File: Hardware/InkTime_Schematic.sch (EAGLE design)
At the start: 105 parts, among them IC1 BQ25180YBGR_BQ25180YBGR, IC2 RT6160AWSC_RT6160AWSC, IC3 BMA423_BMA423, IC4 DRV2605YZFR_DRV2605YZFR, J1 TC2030-IDC_TC2030-IDC, J2 503480-2400_503480-2400, J3 KH-TYPE-C-16P_KH-TYPE-C-16P, P1.01/2.4B NORDIC_NRF_4_NRF52840_QF, Q2 ESP32_C6_LIBRARY_6_SI1308EDL-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, SW1 2025-10-22_07-23-44_LIBRARY_E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, SW2 2025-10-22_07-23-44_LIBRARY_E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, SW3 2025-10-22_07-23-44_LIBRARY_E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, U1 ESP32_C6_LIBRARY_MAX17048G+T10, X1 32MHz, X2 32.768KHz

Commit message: Added GND value to GND objects
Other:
- moved on the sheet: ANT1, C1-EP-DR, C10, C11, C12, C13, C15, C16, C17, C18, C2, C2-EP-DR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

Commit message: redenumire TP
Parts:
- removed TP_SDA1, TP_SDA10, TP_SDA2, TP_SDA3, TP_SDA4, TP_SDA5, TP_SDA6, TP_SDA7, TP_SDA8, TP_SDA9: HECTOR_WATCH_1_TPTP20R, InkTime_v5:HECTOR_WATCH_1_TPTP20R
- added TP_3.3V, TP_BAT_GND, TP_GND, TP_ON, TP_OP, TP_RESET, TP_SWDCLK, TP_SWDIO, TP_SWO, TP_VBAT: HECTOR_WATCH_1_TPTP20R, InkTime_v5:HECTOR_WATCH_1_TPTP20R
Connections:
- net 3V3/2.4A: now also TP_3.3V.TP; no longer TP_SDA5.TP
- net GND: now also TP_BAT_GND.TP, TP_GND.TP; no longer TP_SDA10.TP, TP_SDA6.TP
- net OUT+: now also TP_OP.TP; no longer TP_SDA7.TP
- net OUT-: now also TP_ON.TP; no longer TP_SDA8.TP
- net RESET: now also TP_RESET.TP; no longer TP_SDA4.TP
- net SWDCLK: now also TP_SWDCLK.TP; no longer TP_SDA3.TP
- net SWDIO: now also TP_SWDIO.TP; no longer TP_SDA2.TP
- net SWO: now also TP_SWO.TP; no longer TP_SDA1.TP
- net VBAT/1.2A: now also TP_VBAT.TP; no longer TP_SDA9.TP
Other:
- moved on the sheet: ANT1, C1-EP-DR, C10, C11, C12, C13, C15, C16, C17, C18, C2, C2-EP-DR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

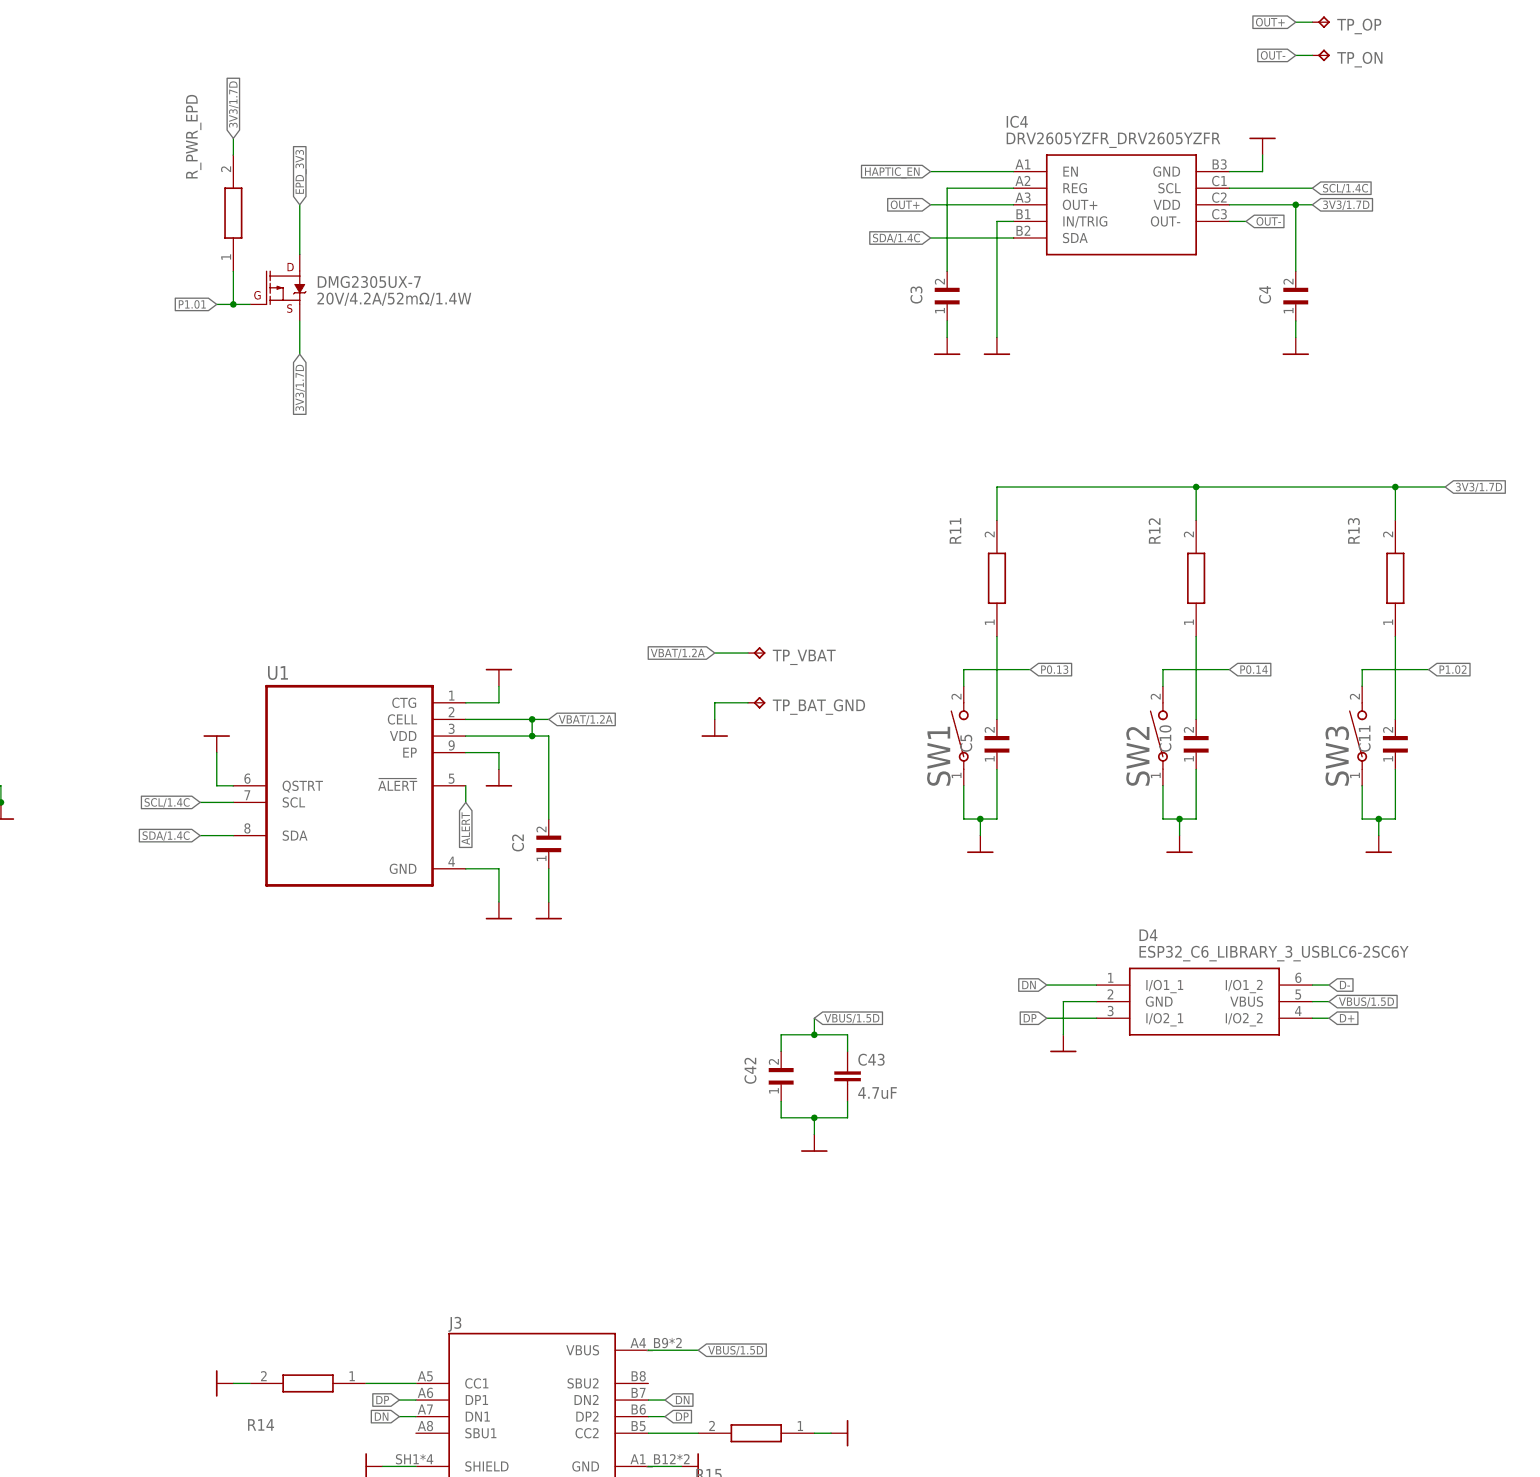
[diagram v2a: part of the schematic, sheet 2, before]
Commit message: added 4 layer pcb variant and fixed schematic broken connections
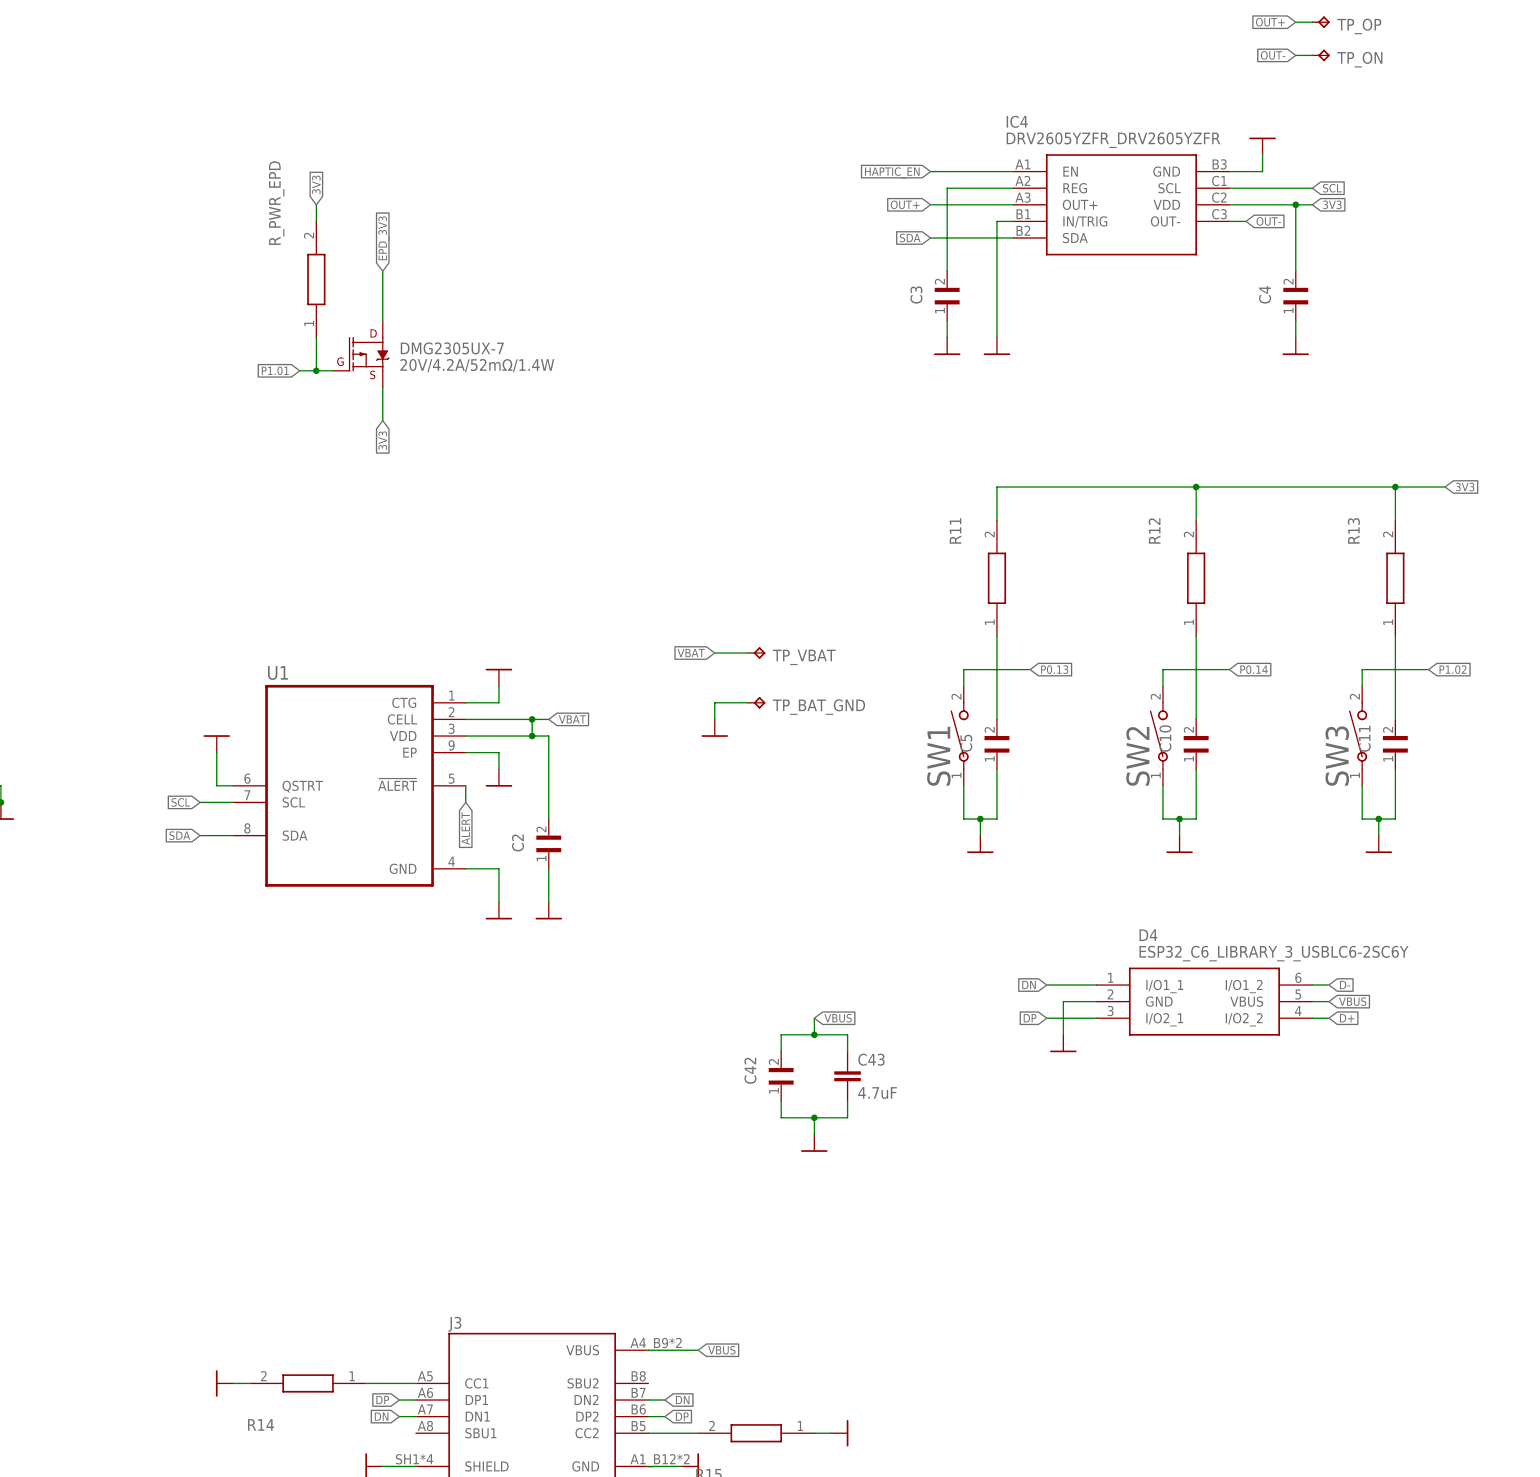
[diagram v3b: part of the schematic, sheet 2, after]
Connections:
- removed net 3V3/1.7D: C4.2, DMG2305UX-7.S, IC4.VDD, R11.2, R12.2, R13.2, R_PWR_EPD.2
- removed net 3V3/2.4A: C25.1, C33.1, C6.2, C7.1, C8.1, CC14.2, CC19.1, IC2.VOUT_1, IC2.VOUT_2, IC3.CSB, IC3.VDD, IC3.VDDIO, J1.1, P1.01/2.4B.VDD@AD14, P1.01/2.4B.VDD@AD23, P1.01/2.4B.VDD@B1, P1.01/2.4B.VDD@W1, P1.01/2.4B.VDDH@Y2, R4.2, R5.2, TP_3.3V.TP, TP_3V3.TP
- removed net SCL/1.4C: IC4.SCL, U1.SCL
- removed net SCL/2.4C: IC1.SCL, IC3.SCX, P1.01/2.4B.P0.07@M2, R2.1, R4.1, TP_SCL.TP
- removed net SDA/1.4C: IC4.SDA, U1.SDA
- removed net SDA/2.4C: IC1.SDA, IC3.SDX, P1.01/2.4B.P0.06@L1, R3.1, R5.1, TP_SDA.TP
- removed net VBAT/1.2A: C2.2, TP_VBAT.TP, U1.CELL, U1.VDD
- removed net VBAT/2.5C: C37.1, IC1.BAT
- removed net VBUS/1.5D: C42.2, C43.1, D4.VBUS, J3.VBUS
- removed net VBUS/2.6D: C21.1, C38.1, IC1.IN, P1.01/2.4B.VBUS@AD2
- new net 3V3: C25.1, C33.1, C4.2, C6.2, C7.1, C8.1, CC14.2, CC19.1, DMG2305UX-7.S, IC2.VOUT_1, IC2.VOUT_2, IC3.CSB, IC3.VDD, IC3.VDDIO, IC4.VDD, J1.1, P1.01/2.4B.VDD@AD14, P1.01/2.4B.VDD@AD23, P1.01/2.4B.VDD@B1, P1.01/2.4B.VDD@W1, P1.01/2.4B.VDDH@Y2, R11.2, R12.2, R13.2, R4.2, R5.2, R_PWR_EPD.2, TP_3.3V.TP, TP_3V3.TP
- new net SCL: IC1.SCL, IC3.SCX, IC4.SCL, P1.01/2.4B.P0.07@M2, R2.1, R4.1, TP_SCL.TP, U1.SCL
- new net SDA: IC1.SDA, IC3.SDX, IC4.SDA, P1.01/2.4B.P0.06@L1, R3.1, R5.1, TP_SDA.TP, U1.SDA
- new net VBAT: C2.2, C37.1, IC1.BAT, TP_VBAT.TP, U1.CELL, U1.VDD
- new net VBUS: C21.1, C38.1, C42.2, C43.1, D4.VBUS, IC1.IN, J3.VBUS, P1.01/2.4B.VBUS@AD2
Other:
- moved on the sheet: DMG2305UX-7, R_PWR_EPD
